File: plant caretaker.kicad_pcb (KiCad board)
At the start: 2 copper layers, 6 parts, among them Q3 FDMS86255, U1 UDA1380HN_N2, U4 LM2596S-5, U5 PAM8403D

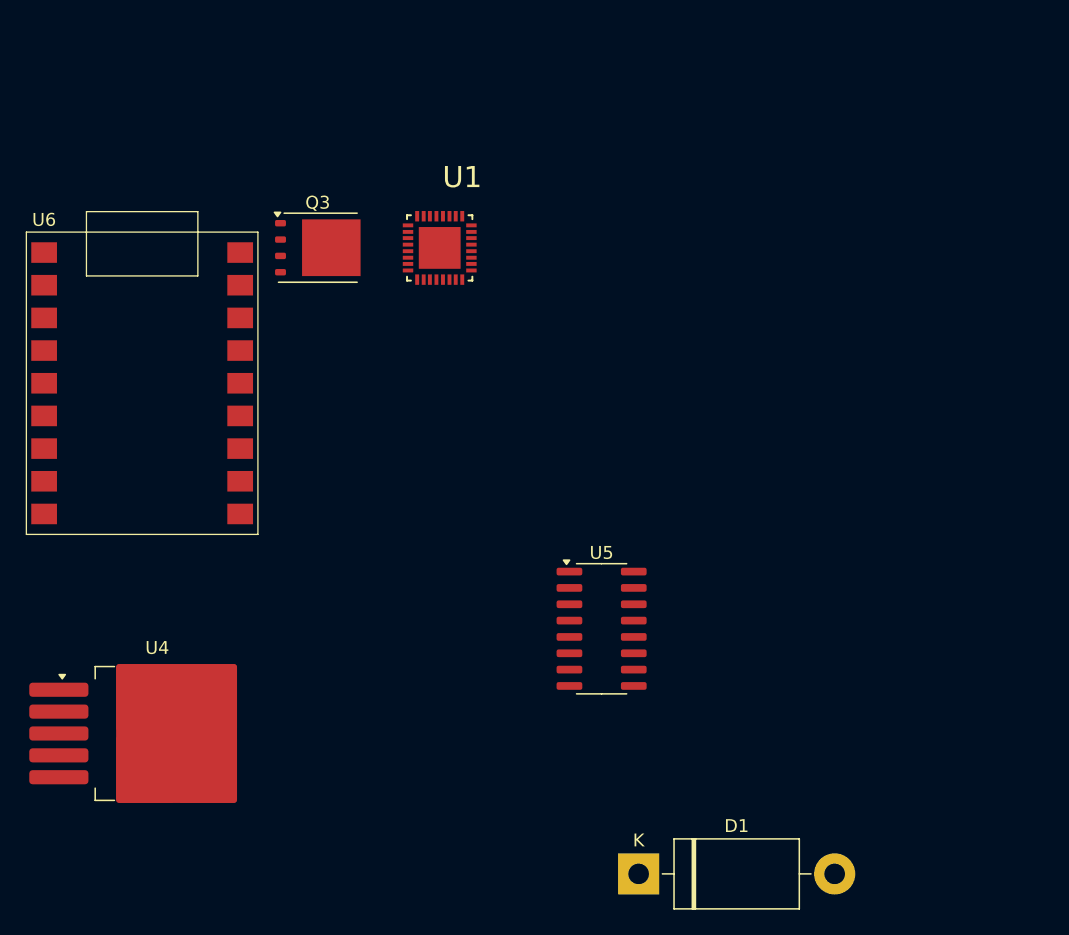
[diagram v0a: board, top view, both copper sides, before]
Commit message: Added footprints and imported to PCB
All of them except speakers
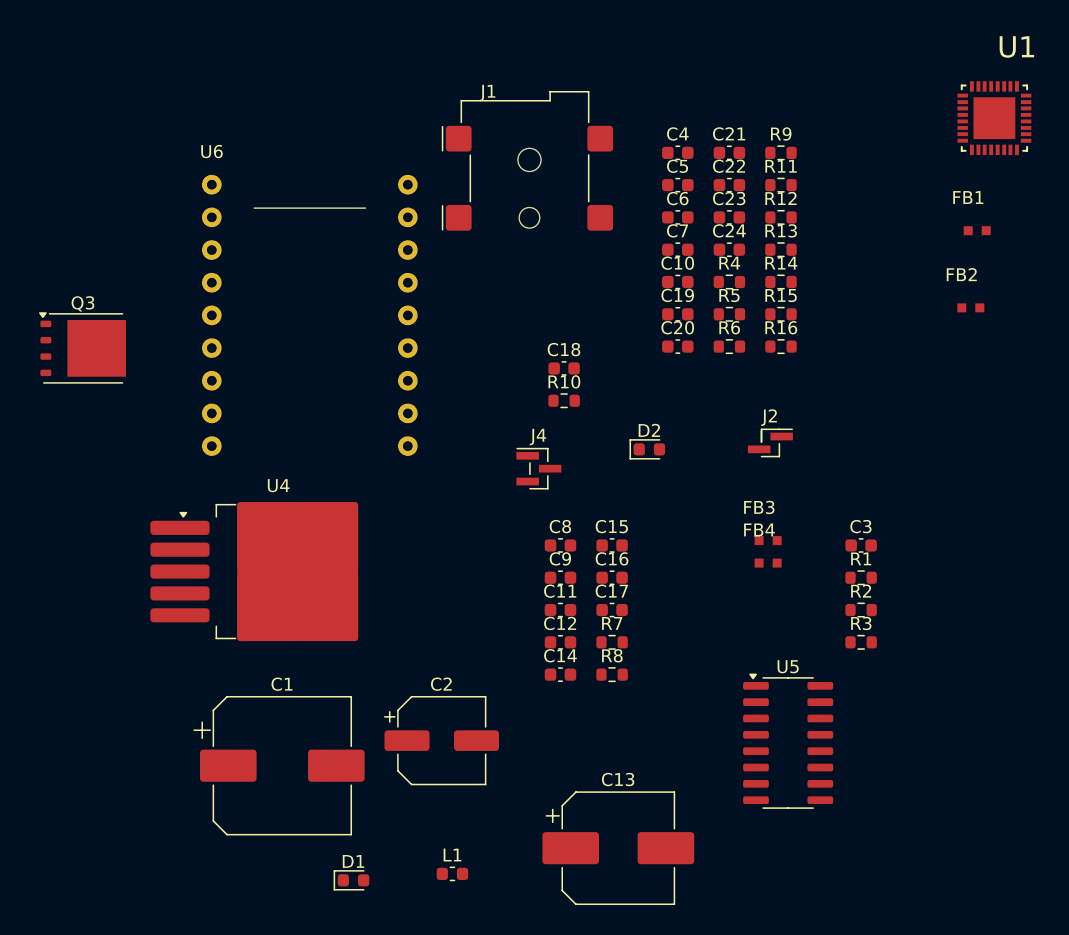
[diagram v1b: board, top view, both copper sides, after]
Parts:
- added C1: 680u, Capacitor_SMD:CP_Elec_10x12.5, F.Cu at (114.2, 99.6)
- added C10: 4.7u, Capacitor_SMD:C_0603_1608Metric, F.Cu at (144.9, 62.0)
- added C11: 1u, Capacitor_SMD:C_0603_1608Metric, F.Cu at (135.8, 87.5)
- added C12: 0.1u, Capacitor_SMD:C_0603_1608Metric, F.Cu at (135.8, 90.0)
- added C13: 470u, Capacitor_SMD:CP_Elec_8x10.5, F.Cu at (140.3, 106.0)
- added C14: 1u, Capacitor_SMD:C_0603_1608Metric, F.Cu at (135.8, 92.5)
- added C15: 0.47u, Capacitor_SMD:C_0603_1608Metric, F.Cu at (139.8, 82.5)
- added C16: 0.47u, Capacitor_SMD:C_0603_1608Metric, F.Cu at (139.8, 85.0)
- added C17: 1u, Capacitor_SMD:C_0603_1608Metric, F.Cu at (139.8, 87.5)
- added C18: 0.01u, Capacitor_SMD:C_0603_1608Metric, F.Cu at (136.1, 68.7)
- added C19: 100u, Capacitor_SMD:C_0603_1608Metric, F.Cu at (144.9, 64.5)
- added C2: 220u, Capacitor_SMD:CP_Elec_6.3x7.7, F.Cu at (126.6, 97.6)
- added C20: 0.1u, Capacitor_SMD:C_0603_1608Metric, F.Cu at (144.9, 67.0)
- added C21: 47u, Capacitor_SMD:C_0603_1608Metric, F.Cu at (148.9, 52.0)
- added C22: 47u, Capacitor_SMD:C_0603_1608Metric, F.Cu at (148.9, 54.5)
- added C23: 0.1u, Capacitor_SMD:C_0603_1608Metric, F.Cu at (148.9, 57.0)
- added C24: 100u, Capacitor_SMD:C_0603_1608Metric, F.Cu at (148.9, 59.5)
- added C3: 0.01u, Capacitor_SMD:C_0603_1608Metric, F.Cu at (159.2, 82.5)
- added C4: 100u, Capacitor_SMD:C_0603_1608Metric, F.Cu at (144.9, 52.0)
- added C5: 100u, Capacitor_SMD:C_0603_1608Metric, F.Cu at (144.9, 54.5)
- added C6: 100u, Capacitor_SMD:C_0603_1608Metric, F.Cu at (144.9, 57.0)
- added C7: 0.1u, Capacitor_SMD:C_0603_1608Metric, F.Cu at (144.9, 59.5)
- added C8: 220p, Capacitor_SMD:C_0603_1608Metric, F.Cu at (135.8, 82.5)
- added C9: 220p, Capacitor_SMD:C_0603_1608Metric, F.Cu at (135.8, 85.0)
- added D2: D, Diode_SMD:D_0603_1608Metric, F.Cu at (142.7, 75.0)
- added FB1: FerriteBead, OtherComponents:FerriteBead_742861160_0603, F.Cu at (167.5, 58.0)
- added FB2: FerriteBead, OtherComponents:FerriteBead_742861160_0603, F.Cu at (167.0, 64.0)
- added FB3: FerriteBead, OtherComponents:FerriteBead_742861160_0603, F.Cu at (151.2, 82.1)
- added FB4: FerriteBead, OtherComponents:FerriteBead_742861160_0603, F.Cu at (151.2, 83.8)
- added J1: 694106402002, Connector_BarrelJack:BarrelJack_Wuerth_694106106102_2.0x5.5mm, F.Cu at (133.4, 53.9)
- added J2: Water_Pump, Connector_PinHeader_1.00mm:PinHeader_1x02_P1.00mm_Vertical_SMD_Pin1Right, F.Cu at (152.1, 74.5)
- added J4: Kitronik, Connector_PinHeader_1.00mm:PinHeader_1x03_P1.00mm_Vertical_SMD_Pin1Left, F.Cu at (134.1, 76.5)
- added L1: 33u, Inductor_SMD:L_0603_1608Metric, F.Cu at (127.4, 108.0)
- added R1: 4.7k, Resistor_SMD:R_0603_1608Metric, F.Cu at (159.2, 85.0)
- added R10: 1k, Resistor_SMD:R_0603_1608Metric, F.Cu at (136.1, 71.2)
- added R11: 1, Resistor_SMD:R_0603_1608Metric, F.Cu at (152.9, 54.5)
- added R12: 47, Resistor_SMD:R_0603_1608Metric, F.Cu at (152.9, 57.0)
- added R13: 10k, Resistor_SMD:R_0603_1608Metric, F.Cu at (152.9, 59.5)
- added R14: 10k, Resistor_SMD:R_0603_1608Metric, F.Cu at (152.9, 62.0)
- added R15: 100, Resistor_SMD:R_0603_1608Metric, F.Cu at (152.9, 64.5)
- added R16: 100, Resistor_SMD:R_0603_1608Metric, F.Cu at (152.9, 67.0)
- added R2: 4.7k, Resistor_SMD:R_0603_1608Metric, F.Cu at (159.2, 87.5)
- added R3: 4.7k, Resistor_SMD:R_0603_1608Metric, F.Cu at (159.2, 90.0)
- added R4: 100, Resistor_SMD:R_0603_1608Metric, F.Cu at (148.9, 62.0)
- added R5: 10k, Resistor_SMD:R_0603_1608Metric, F.Cu at (148.9, 64.5)
- added R6: 47k, Resistor_SMD:R_0603_1608Metric, F.Cu at (148.9, 67.0)
- added R7: R, Resistor_SMD:R_0603_1608Metric, F.Cu at (139.8, 90.0)
- added R8: R, Resistor_SMD:R_0603_1608Metric, F.Cu at (139.8, 92.5)
- added R9: 10, Resistor_SMD:R_0603_1608Metric, F.Cu at (152.9, 52.0)
- D1: footprint Diode_THT:D_DO-201AD_P15.24mm_Horizontal -> Diode_SMD:D_0603_1608Metric
- U6: value ~ -> ESP32_C3_ZERO
- moved U1 44.3 mm to (169.5, 49.3)
- moved D1 22.2 mm to (119.7, 108.5)
- moved Q3 19.8 mm to (98.7, 67.2)
- moved U5 17.0 mm to (153.5, 97.8)
- moved U4 15.7 mm to (113.9, 84.5)
- moved U6 14.1 mm to (108.7, 54.4)

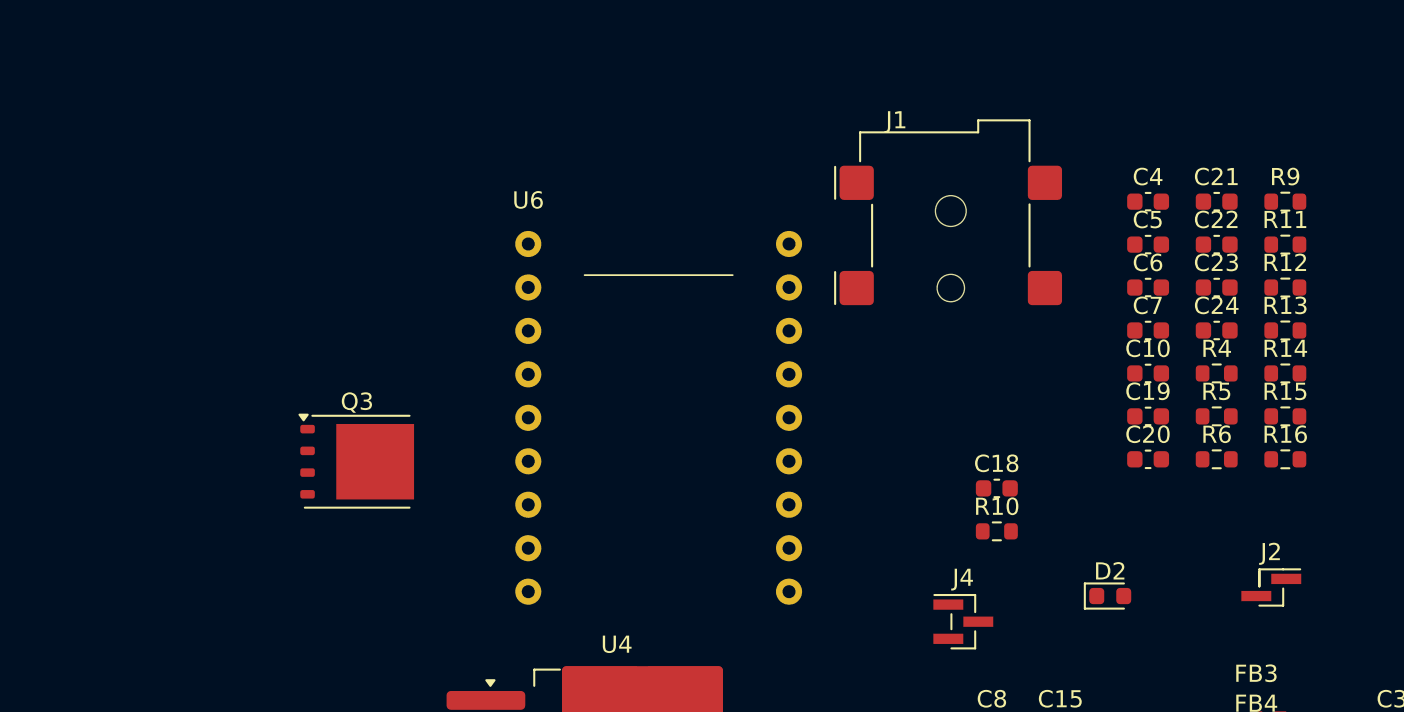
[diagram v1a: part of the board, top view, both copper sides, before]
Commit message: Moved footprints to proper folder
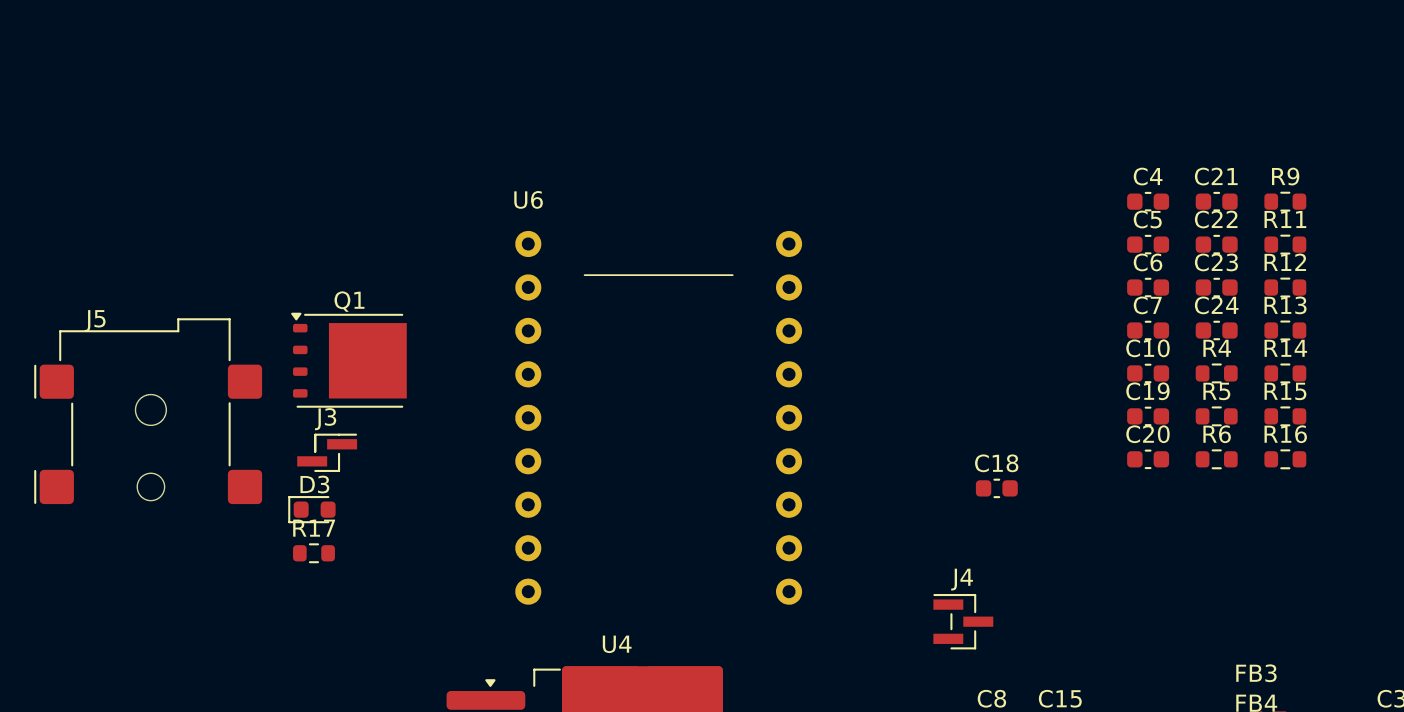
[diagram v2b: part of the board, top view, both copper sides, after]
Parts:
- removed D2: D, Diode_SMD:D_0603_1608Metric
- removed J1: 694106402002, Connector_BarrelJack:BarrelJack_Wuerth_694106106102_2.0x5.5mm
- removed J2: Water_Pump, Connector_PinHeader_1.00mm:PinHeader_1x02_P1.00mm_Vertical_SMD_Pin1Right
- removed Q3: FDMS86255, Package_TO_SOT_SMD:TDSON-8-1
- removed R10: 1k, Resistor_SMD:R_0603_1608Metric
- added D3: D, Diode_SMD:D_0603_1608Metric, F.Cu at (96.2, 70.0)
- added J3: Water_Pump, Connector_PinHeader_1.00mm:PinHeader_1x02_P1.00mm_Vertical_SMD_Pin1Right, F.Cu at (96.9, 66.6)
- added J5: 694106402002, Connector_BarrelJack:BarrelJack_Wuerth_694106106102_2.0x5.5mm, F.Cu at (86.6, 65.5)
- added Q1: FDMS86255, Package_TO_SOT_SMD:TDSON-8-1, F.Cu at (98.3, 61.2)
- added R17: 1k, Resistor_SMD:R_0603_1608Metric, F.Cu at (96.2, 72.5)
- R7, R8: value R -> 18k
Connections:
- net /BuckConverter/12V_IN renamed Net-(D3-K)
- U6 pad 18: Net-(U6-GPIO21) -> /BuckConverter/PWM_IN

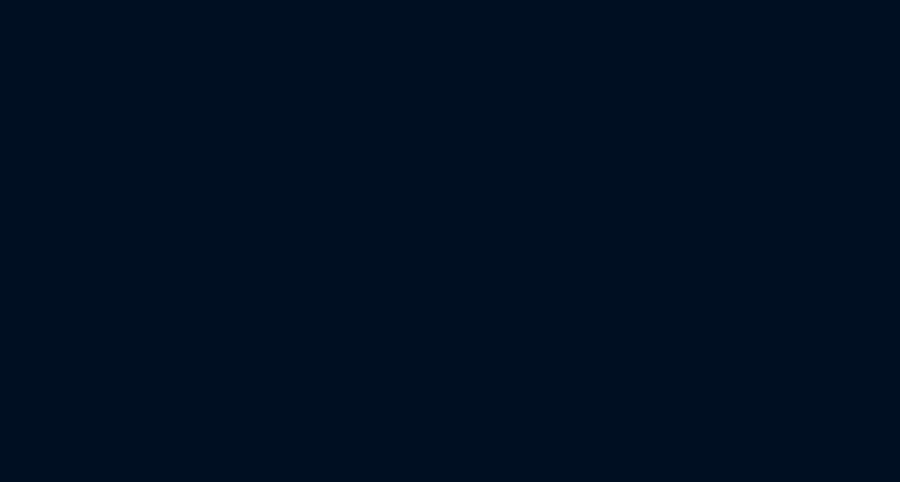
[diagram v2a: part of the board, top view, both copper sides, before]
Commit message: Added TMP157 footprint
Fixed and added the rest of footprints to the PCB
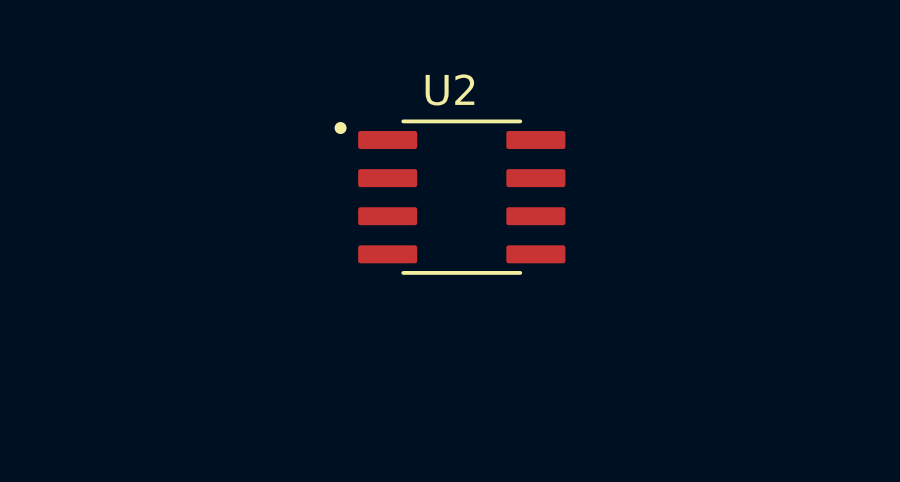
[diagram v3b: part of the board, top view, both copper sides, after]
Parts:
- added U2: TMP175AIDR, TMP175AIDR:TMP-SOIC127P599X175-8N, F.Cu at (127.5, 41.1)

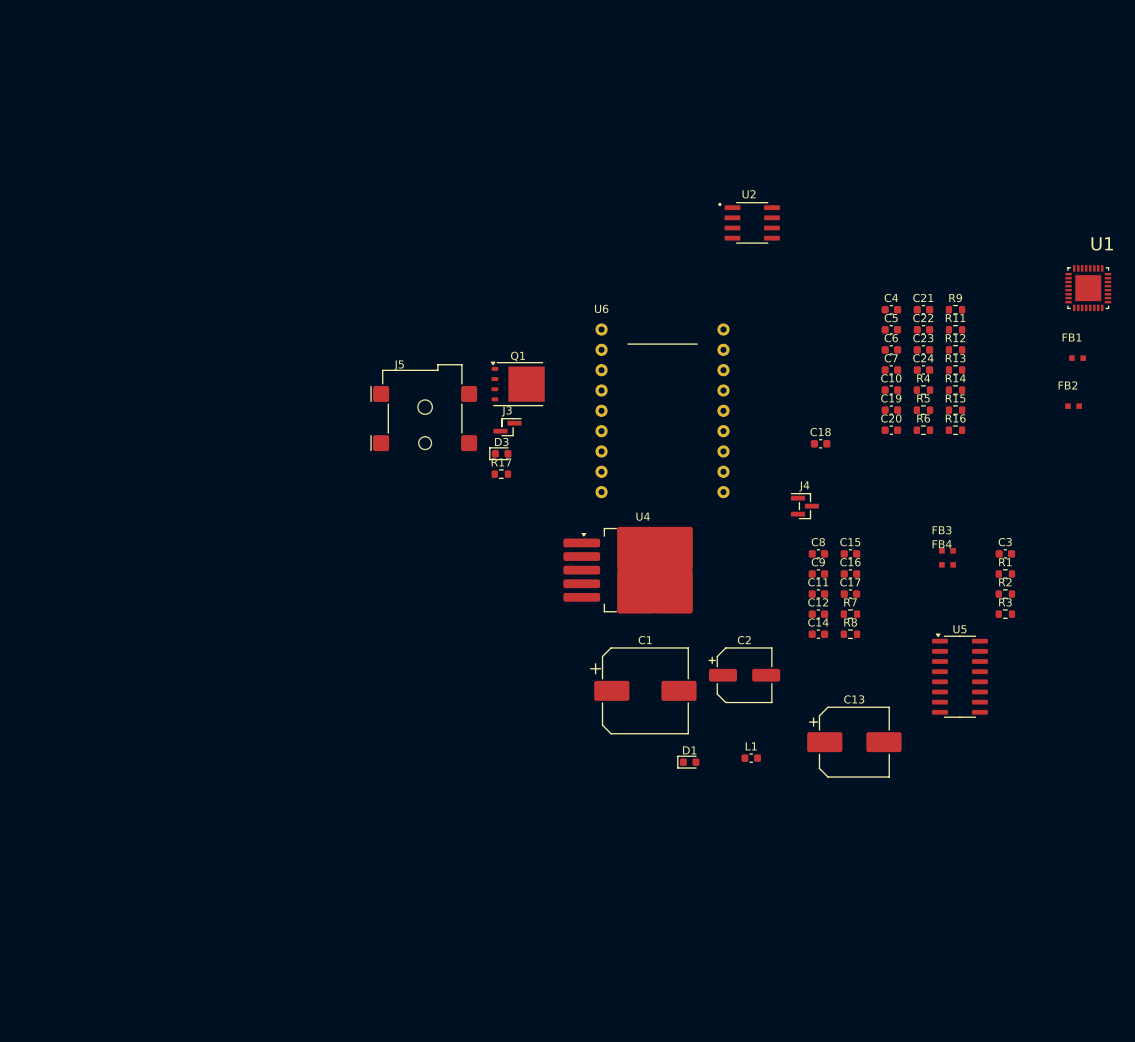
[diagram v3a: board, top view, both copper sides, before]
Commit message: Imported design rules
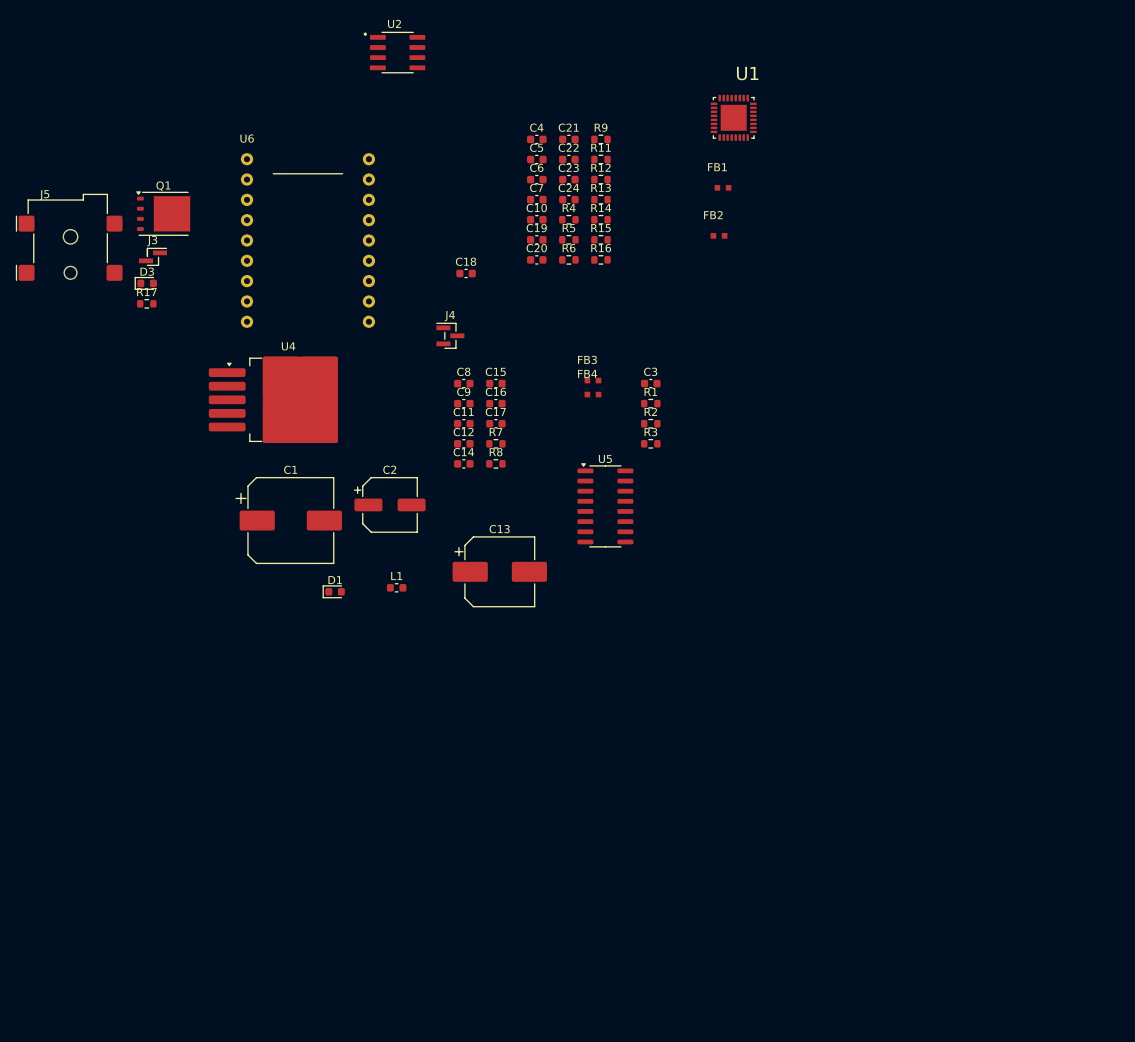
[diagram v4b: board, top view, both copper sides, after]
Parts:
- moved C1 49.2 mm to (69.9, 78.3)
- moved C12 49.2 mm to (91.5, 68.7)
- moved C13 49.2 mm to (96.0, 84.7)
- moved C14 49.2 mm to (91.5, 71.2)
- moved C2 49.2 mm to (82.3, 76.3)
- moved C20 49.2 mm to (100.6, 45.7)
- moved C21 49.2 mm to (104.6, 30.7)
- moved C4 49.2 mm to (100.6, 30.7)
- moved C9 49.2 mm to (91.5, 63.7)
- moved D1 49.2 mm to (75.4, 87.2)
- moved FB3 49.2 mm to (106.9, 60.8)
- moved FB4 49.2 mm to (106.9, 62.5)
- moved L1 49.2 mm to (83.1, 86.7)
- moved R1 49.2 mm to (114.9, 63.7)
- moved R3 49.2 mm to (114.9, 68.7)
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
